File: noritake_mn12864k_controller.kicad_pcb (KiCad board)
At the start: 4 copper layers, 99 x 46.5 mm, 185 parts, among them J1 Conn_01x11, J2 USB_C_Receptacle_USB2.0, J3 TagConnect_TC2030_SWD, J4 Conn_01x18, Q1 AO3400A, Q10 2N7002, Q11 LBSS84LT1G, Q12 2N7002, Q13 TO-252, Q14 CJT04N15, Q15 2N7002, Q16 LBSS84LT1G, Q17 2N7002, Q18 S9015, Q2 AO3400A, Q3 S9015, Q4 AO3401A, Q5 AO3401A, Q6 S9015, Q7 2N7002, Q8 LBSS84LT1G, Q9 2N7002, T1 Wuerth 760390013, T2 Wuerth 760390013, T3 Wuerth 760390013, T4 Wuerth 760390013, U1 SN74AVC8T245PW, U10 SRV05-4, U11 SRV05-4, U12 SRV05-4, U2 74HC14, U3 CD4051B, U4 MN12864K, U5 STM32F730R8T6, U6 NE555D, U7 74HC08, U8 SRV05-4, U9 XC6206PxxxMR

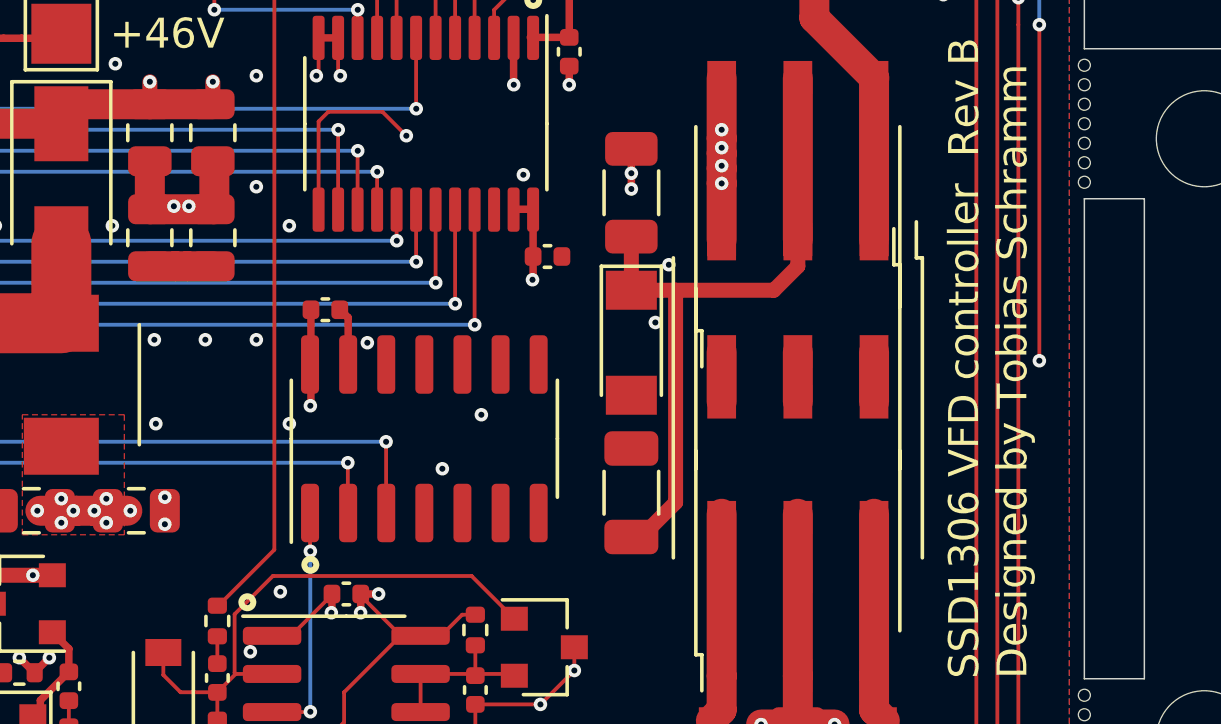
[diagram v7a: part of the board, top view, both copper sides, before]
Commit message: Add more VFD VDD2 bypassing
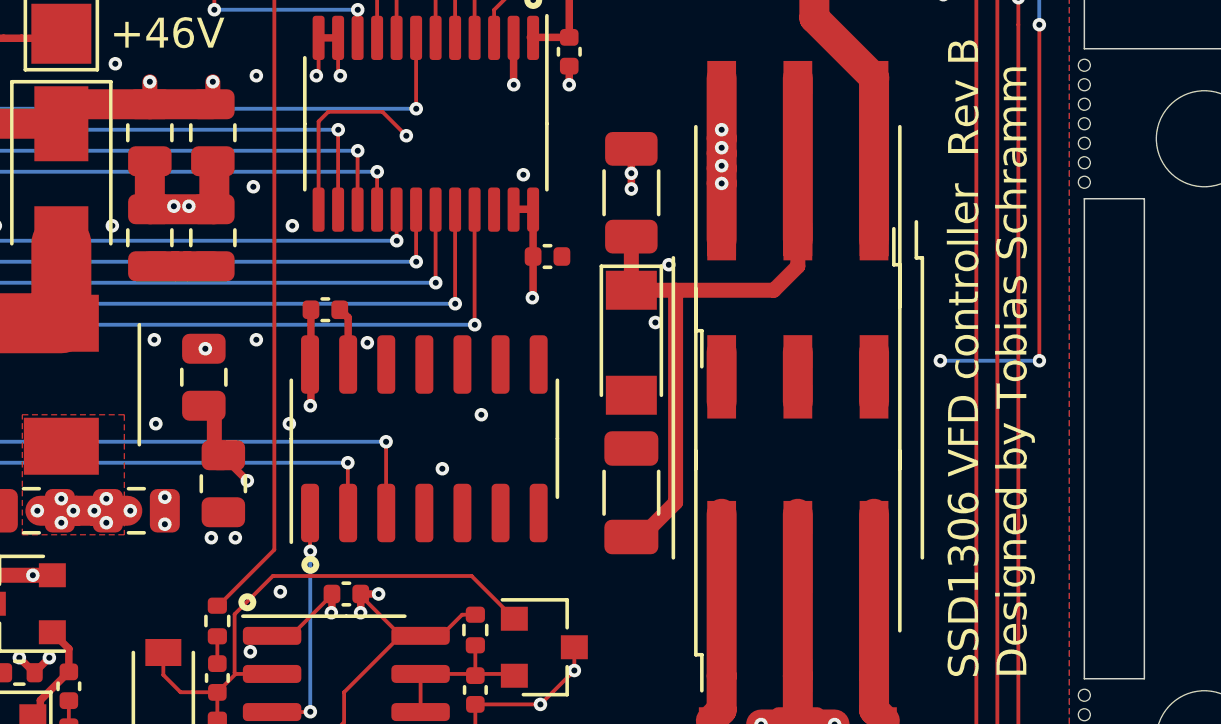
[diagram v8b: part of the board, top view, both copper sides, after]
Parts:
- added C42: 10uF, Capacitor_SMD:C_0805_2012Metric, F.Cu at (155.7, 113.5)
- added C43: 10uF, Capacitor_SMD:C_0805_2012Metric, F.Cu at (156.3, 117.0)
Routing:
- net Net-(C30-Pad1): track 23.5 -> 39.6 mm, vias 4 -> 5
- net +3V3: track 93.9 -> 105.0 mm, vias 17 -> 18
- net +48V: track 41.7 -> 48.9 mm, vias 4 -> 5
- net GND: vias 147 -> 148
